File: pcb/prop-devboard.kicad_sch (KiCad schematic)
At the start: 0 parts

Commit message: Initial work on PCB
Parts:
- added C10, C7: 100nF, Capacitor_SMD:C_0402_1005Metric, symbol Device:C
- added C3, C4: 10pF, Capacitor_SMD:C_0402_1005Metric, symbol Device:C
- added C5, C6: 12pF, Capacitor_SMD:C_0402_1005Metric, symbol Device:C
- added R3: 10k, Resistor_SMD:R_0402_1005Metric, symbol Device:R
- added SW1: SW_Push, Button_Switch_SMD:SW_SPST_B3U-1000P, symbol Switch:SW_Push
- added U1: STM32G0B1CBT6, Package_QFP:LQFP-48_7x7mm_P0.5mm, symbol MCU_ST_STM32G0:STM32G0B1CBTx
- added Y1: 32.768 KHz, 10ppm, 12.5pf, Crystal:Crystal_SMD_3215-2Pin_3.2x1.5mm, symbol Device:Crystal
- added Y2: 8 MHz, 10ppm, 10pf, Crystal:Crystal_SMD_3225-4Pin_3.2x2.5mm, symbol Device:Crystal_GND24
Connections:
- new net +3V3: C7.1, R3.1, U1.6 (VDD)
- new net GND: C10.1, C3.2, C4.2, C5.1, C6.2, C7.2, SW1.1, U1.7 (VSS), Y2.2, Y2.4
- new net NRST: C10.2, R3.2, SW1.2, U1.10 (PF2)
- new net OSC32_IN: C5.2, U1.2 (PC14), Y1.2
- new net OSC32_OUT: C6.1, U1.3 (PC15), Y1.1
- new net OSC_IN: C3.1, U1.8 (PF0), Y2.1
- new net OSC_OUT: C4.1, U1.9 (PF1), Y2.3
- new net SWCLK: U1.36 (PA14)
- new net SWDIO: U1.35 (PA13)
- new net UART_RX: U1.32 (PA10/UCPD1_DBCC2)
- new net UART_TX: U1.29 (PA9/UCPD1_DBCC1)
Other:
- added sheet Connectors (connectors.kicad_sch)
- added sheet Power (power.kicad_sch)

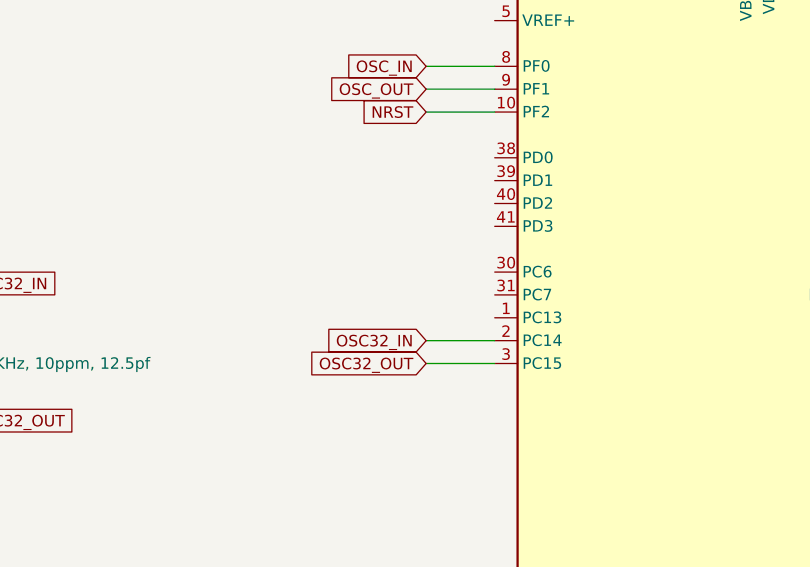
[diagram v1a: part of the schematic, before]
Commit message: Added CubeMX template, and more schematics work
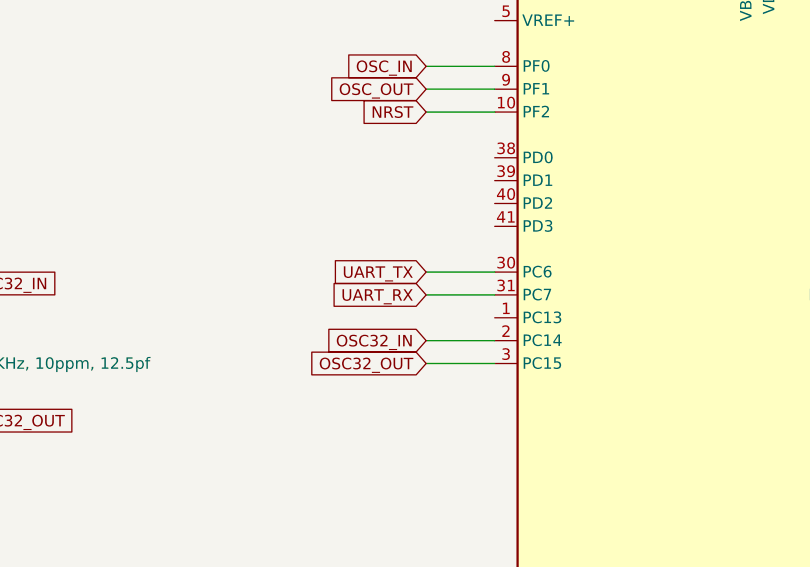
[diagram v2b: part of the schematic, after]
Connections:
- net UART_RX: now also U1.31 (PC7)
- net UART_TX: now also U1.30 (PC6)
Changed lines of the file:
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@@
+	(wire
+		(pts
+			(xy 189.23 74.93) (xy 196.85 74.93)
+		)
+		(stroke
+			(width 0)
+			(type default)
+		)
+	)
 	(wire
 		(pts
@@
 	(wire
 		(pts
+			(xy 189.23 77.47) (xy 196.85 77.47)
+		)
+		(stroke
+			(width 0)
+			(type default)
+		)
+	)
+	(wire
+		(pts
 			(xy 227.33 27.94) (xy 227.33 31.75)
 		)
@@
 		)
 	)
+	(global_label "UART_RX"
+		(shape input)
+		(at 189.23 77.47 180)
+		(fields_autoplaced yes)
+		(effects
+			(font
+				(size 1.27 1.27)
+			)
+			(justify right)
+		)
+		(property "Intersheetrefs" "${INTERSHEET_REFS}"
+			(at 178.141 77.47 0)
+			(effects
+				(font
+					(size 1.27 1.27)
+				)
+				(justify right)
+				(hide yes)
+			)
+		)
+	)
 	(global_label "NRST"
 		(shape input)
@@
 				(hide yes)
 			)
+		)
+	)
+	(global_label "UART_TX"
+		(shape input)
+		(at 189.23 74.93 180)
+		(fields_autoplaced yes)
+		(effects
+			(font
+				(size 1.27 1.27)
+			)
+			(justify right)
+		)
+		(property "Intersheetrefs" "${INTERSHEET_REFS}"
+			(at 178.4434 74.93 0)
+			(effects
+				(font
+					(size 1.27 1.27)
+				)
+				(justify right)
+				(hide yes)
+			)

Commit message: Lots of work on schematics
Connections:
- net UART_RX: no longer U1.32 (PA10/UCPD1_DBCC2)
- net UART_TX: no longer U1.29 (PA9/UCPD1_DBCC1)
- net ANALOG0: now reaches U1.11 (PA0)
- net ANALOG1: now reaches U1.12 (PA1)
- net ANALOG2: now reaches U1.13 (PA2)
- net ANALOG3: now reaches U1.14 (PA3)
- net ANALOG4: now reaches U1.15 (PA4)
- net ANALOG5: now reaches U1.16 (PA5)
- net SPI_MISO: now reaches U1.21 (PB2)
- net SPI_SCK: now reaches U1.22 (PB10)
- net SPI_MOSI: now reaches U1.23 (PB11)
- net I2C2_SCL: now reaches U1.25 (PB13)
- net I2C2_SDA: now reaches U1.26 (PB14)
- net I2C3_SCL: now reaches U1.42 (PB3)
- net I2C3_SDA: now reaches U1.43 (PB4)
- new net I2C1_SCL: U1.29 (PA9/UCPD1_DBCC1)
- new net I2C1_SDA: U1.32 (PA10/UCPD1_DBCC2)

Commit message: Mostly finished PCB layout
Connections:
- net DIGITAL5: now reaches U1.33 (PA9/PA11)
- net DIGITAL6: now reaches U1.34 (PA10/PA12)
- net DIGITAL9: now reaches U1.37 (PA15)
- net DIGITAL10: now reaches U1.38 (PD0)
- net DIGITAL11: now reaches U1.39 (PD1)
- net DIGITAL12: now reaches U1.40 (PD2)
- net DIGITAL13: now reaches U1.41 (PD3)
- net SWCLK renamed BOOT0

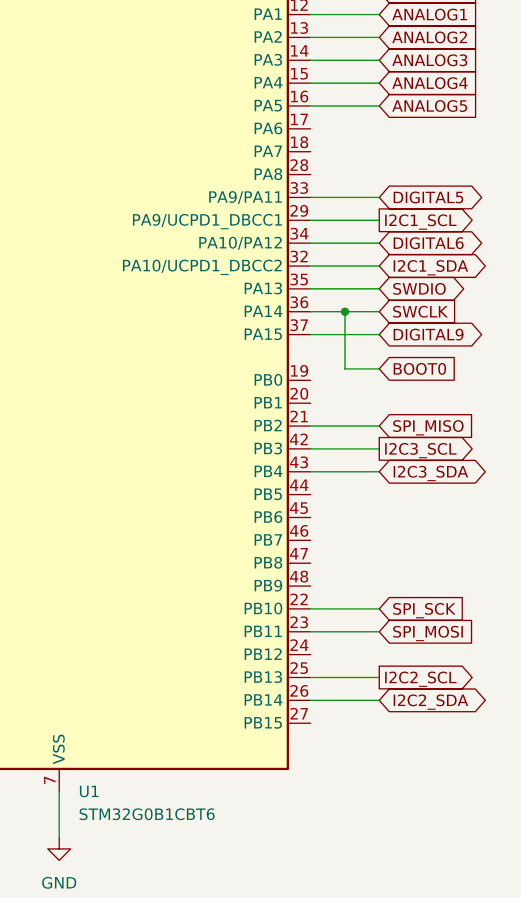
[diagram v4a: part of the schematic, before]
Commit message: Added USB support
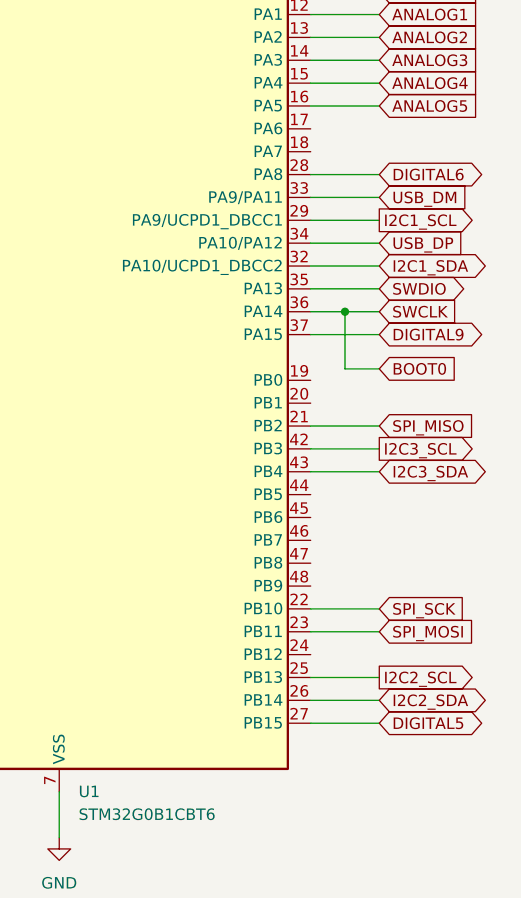
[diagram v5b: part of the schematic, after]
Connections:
- net DIGITAL5: now also U1.27 (PB15); no longer U1.33 (PA9/PA11)
- net DIGITAL6: now also U1.28 (PA8); no longer U1.34 (PA10/PA12)
- new net USB_DM: U1.33 (PA9/PA11)
- new net USB_DP: U1.34 (PA10/PA12)
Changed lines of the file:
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@@
+	(wire
+		(pts
+			(xy 252.73 67.31) (xy 260.35 67.31)
+		)
+		(stroke
+			(width 0)
+			(type default)
+		)
+	)
 	(wire
 		(pts
@@
 	(wire
 		(pts
+			(xy 252.73 128.27) (xy 260.35 128.27)
+		)
+		(stroke
+			(width 0)
+			(type default)
+		)
+	)
+	(wire
+		(pts
 			(xy 189.23 62.23) (xy 196.85 62.23)
 		)
@@
 		(property "Intersheetrefs" "${INTERSHEET_REFS}"
 			(at 146.8581 118.11 0)
+			(effects
+				(font
+					(size 1.27 1.27)
+				)
+				(justify left)
+				(hide yes)
+			)
+		)
+	)
+	(global_label "DIGITAL6"
+		(shape bidirectional)
+		(at 260.35 67.31 0)
+		(fields_autoplaced yes)
+		(effects
+			(font
+				(size 1.27 1.27)
+			)
+			(justify left)
+		)
+		(property "Intersheetrefs" "${INTERSHEET_REFS}"
+			(at 272.4899 67.31 0)
 			(effects
 				(font
@@
 		)
 	)
-	(global_label "DIGITAL6"
-		(shape bidirectional)
-		(at 260.35 74.93 0)
-		(fields_autoplaced yes)
-		(effects
-			(font
-				(size 1.27 1.27)
-			)
-			(justify left)
-		)
-		(property "Intersheetrefs" "${INTERSHEET_REFS}"
-			(at 272.4899 74.93 0)
-			(effects
-				(font
-					(size 1.27 1.27)
-				)
-				(justify left)
-				(hide yes)
-			)
-		)
-	)
 	(global_label "I2C3_SCL"
 		(shape output)
@@
 		)
 	)
+	(global_label "USB_DP"
+		(shape input)
+		(at 260.35 74.93 0)
+		(fields_autoplaced yes)
+		(effects
+			(font
+				(size 1.27 1.27)
+			)
+			(justify left)
+		)
+		(property "Intersheetrefs" "${INTERSHEET_REFS}"
+			(at 270.6528 74.93 0)
+			(effects
+				(font
+					(size 1.27 1.27)
+				)
+				(justify left)
+				(hide yes)
+			)
+		)
+	)
 	(global_label "ANALOG3"
 		(shape input)
@@
 		(property "Intersheetrefs" "${INTERSHEET_REFS}"
 			(at 271.681 57.15 0)
+			(effects
+				(font
+					(size 1.27 1.27)
+				)
+				(justify left)
+				(hide yes)
+			)
+		)
+	)
+	(global_label "DIGITAL5"
+		(shape bidirectional)
+		(at 260.35 128.27 0)
+		(fields_autoplaced yes)
+		(effects
+			(font
+				(size 1.27 1.27)
+			)
+			(justify left)
+		)
+		(property "Intersheetrefs" "${INTERSHEET_REFS}"
+			(at 272.4899 128.27 0)
 			(effects
 				(font
@@
 		)
 	)
-	(global_label "DIGITAL5"
-		(shape bidirectional)
-		(at 260.35 69.85 0)
-		(fields_autoplaced yes)
-		(effects
-			(font
-				(size 1.27 1.27)
-			)
-			(justify left)
-		)
-		(property "Intersheetrefs" "${INTERSHEET_REFS}"
-			(at 272.4899 69.85 0)
-			(effects
-				(font
-					(size 1.27 1.27)
-				)
-				(justify left)
-				(hide yes)
-			)
-		)
-	)
 	(global_label "I2C2_SCL"
 		(shape output)
@@
 			(effects
 				(font
+					(size 1.27 1.27)
+				)
+				(justify left)
+				(hide yes)
+			)
+		)
+	)
+	(global_label "USB_DM"
+		(shape input)
+		(at 260.35 69.85 0)
+		(fields_autoplaced yes)
+		(effects
+			(font
+				(size 1.27 1.27)
+			)
+			(justify left)
+		)
+		(property "Intersheetrefs" "${INTERSHEET_REFS}"
+			(at 270.8342 69.85 0)
+			(effects
+				(font

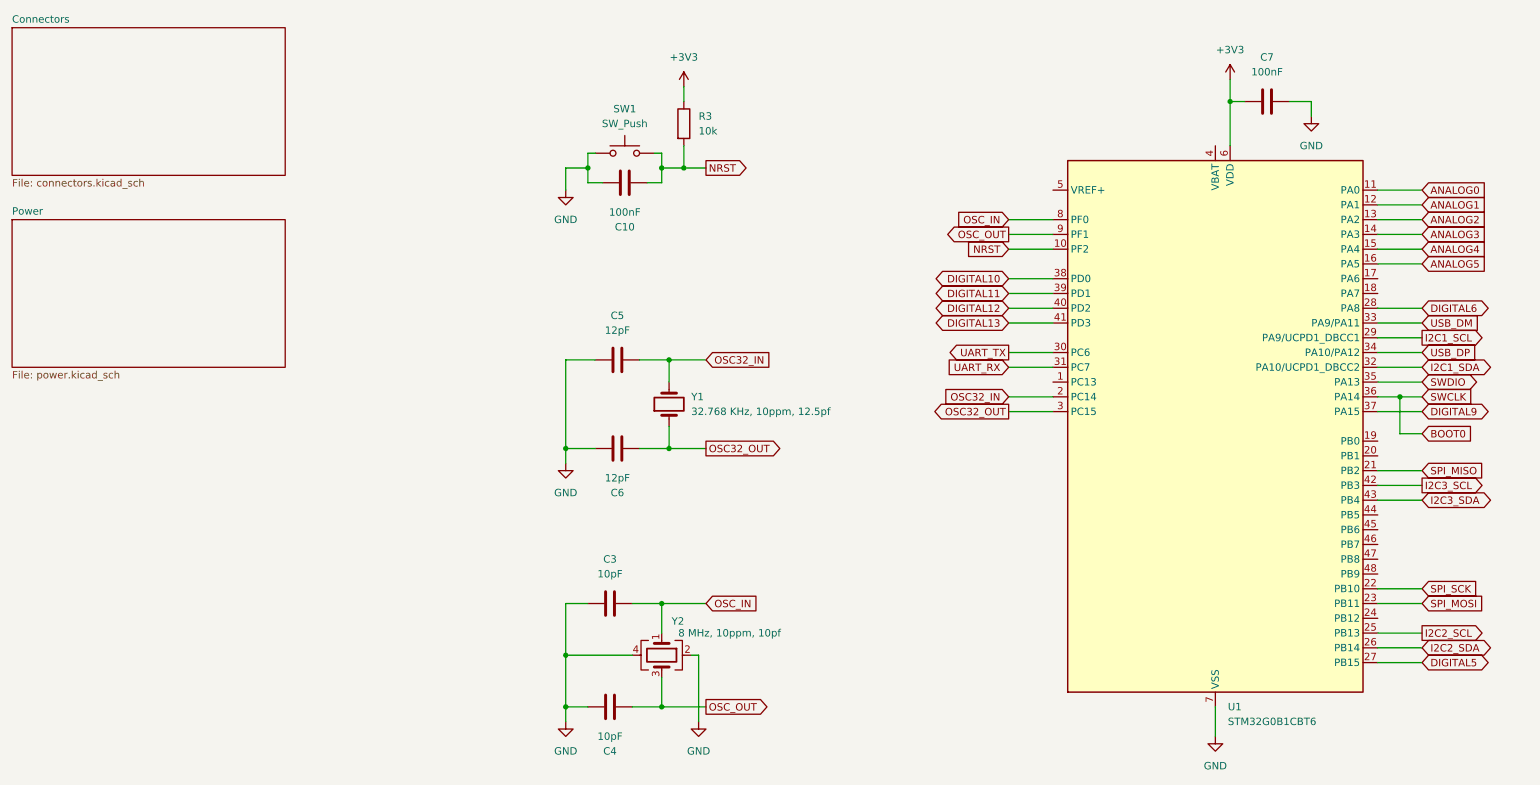
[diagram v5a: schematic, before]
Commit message: Added power and status LEDs to the design
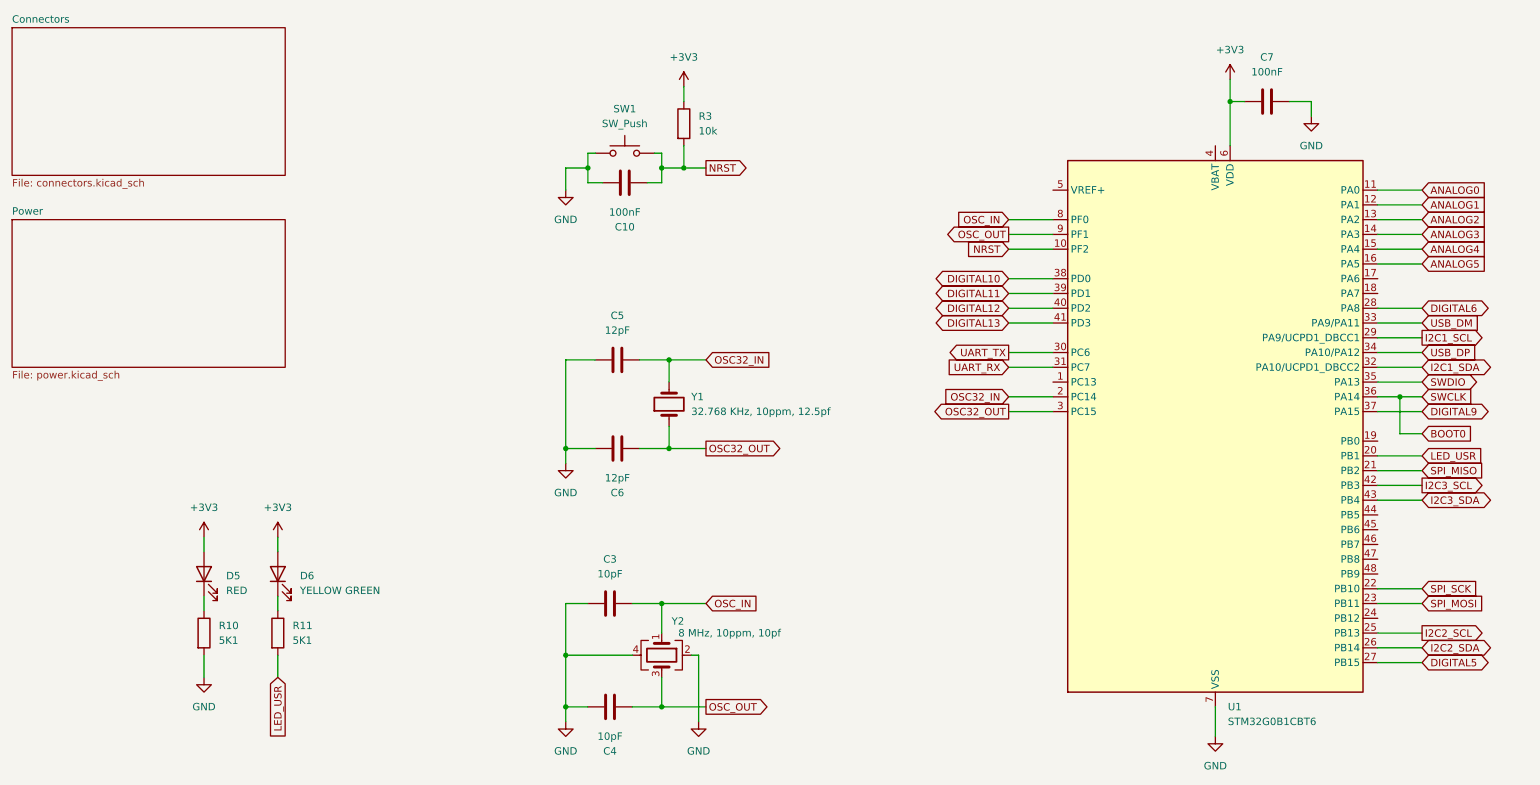
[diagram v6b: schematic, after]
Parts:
- added D5: RED, LED_SMD:LED_0402_1005Metric, symbol Device:LED
- added D6: YELLOW GREEN, LED_SMD:LED_0402_1005Metric, symbol Device:LED
- added R10, R11: 5K1, Resistor_SMD:R_0402_1005Metric, symbol Device:R
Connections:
- net +3V3: now also D5.2 (A), D6.2 (A)
- net GND: now also R10.2
- net LED_USR: now reaches U1.20 (PB1)
- net LED_USR: now also R11.2
- new net: D6.1 (K), R11.1
- new net: D5.1 (K), R10.1

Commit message: Fixed MCU power pins not being connected correctly
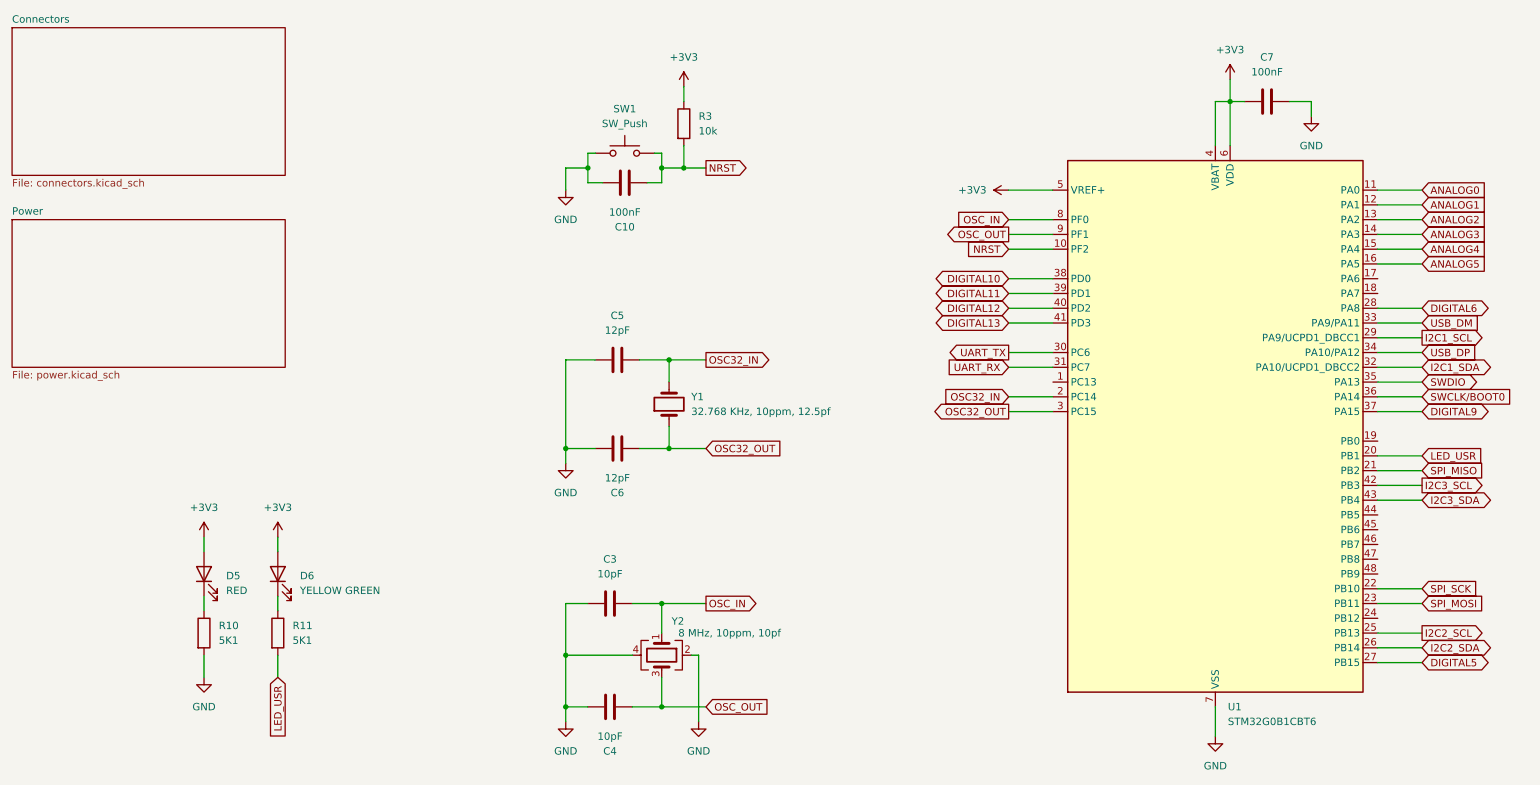
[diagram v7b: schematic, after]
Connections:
- net +3V3: now also U1.4 (VBAT), U1.5 (VREF+)
- net BOOT0 renamed SWCLK/BOOT0
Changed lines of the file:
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@@
 	(paper "A4")
-	(junction
-		(at 256.54 82.55)
-		(diameter 0)
-		(color 0 0 0 0)
-	)
 	(junction
 		(at 129.54 135.89)
@@
 	(wire
 		(pts
+			(xy 224.79 39.37) (xy 224.79 31.75)
+		)
+		(stroke
+			(width 0)
+			(type default)
+		)
+	)
+	(wire
+		(pts
 			(xy 50.8 106.68) (xy 50.8 109.22)
 		)
@@
 	(wire
 		(pts
-			(xy 260.35 88.9) (xy 256.54 88.9)
-		)
-		(stroke
-			(width 0)
-			(type default)
-		)
-	)
-	(wire
-		(pts
 			(xy 189.23 74.93) (xy 196.85 74.93)
 		)
@@
 	(wire
 		(pts
-			(xy 256.54 88.9) (xy 256.54 82.55)
-		)
-		(stroke
-			(width 0)
-			(type default)
-		)
-	)
-	(wire
-		(pts
 			(xy 129.54 43.18) (xy 133.35 43.18)
 		)
@@
 	(wire
 		(pts
+			(xy 224.79 31.75) (xy 227.33 31.75)
+		)
+		(stroke
+			(width 0)
+			(type default)
+		)
+	)
+	(wire
+		(pts
 			(xy 116.84 45.72) (xy 119.38 45.72)
 		)
@@
 	(wire
 		(pts
-			(xy 256.54 82.55) (xy 260.35 82.55)
+			(xy 252.73 82.55) (xy 260.35 82.55)
 		)
 		(stroke
@@
 	(wire
 		(pts
+			(xy 189.23 46.99) (xy 196.85 46.99)
+		)
+		(stroke
+			(width 0)
+			(type default)
+		)
+	)
+	(wire
+		(pts
 			(xy 237.49 31.75) (xy 241.3 31.75)
 		)
@@
 	(wire
 		(pts
-			(xy 252.73 82.55) (xy 256.54 82.55)
-		)
-		(stroke
-			(width 0)
-			(type default)
-		)
-	)
-	(wire
-		(pts
 			(xy 252.73 128.27) (xy 260.35 128.27)
 		)
@@
 	)
 	(global_label "OSC_IN"
-		(shape input)
+		(shape output)
 		(at 137.16 118.11 0)
 		(fields_autoplaced yes)
@@
 		)
 	)
-	(global_label "BOOT0"
+	(global_label "OSC_OUT"
 		(shape input)
-		(at 260.35 88.9 0)
-		(fields_autoplaced yes)
-		(effects
-			(font
-				(size 1.27 1.27)
-			)
-			(justify left)
-		)
-		(property "Intersheetrefs" "${INTERSHEET_REFS}"
-			(at 269.4433 88.9 0)
-			(effects
-				(font
-					(size 1.27 1.27)
-				)
-				(justify left)
-				(hide yes)
-			)
-		)
-	)
-	(global_label "OSC_OUT"
-		(shape output)
 		(at 137.16 135.89 0)
 		(fields_autoplaced yes)
@@
 	)
 	(global_label "OSC32_OUT"
-		(shape output)
+		(shape input)
 		(at 137.16 91.44 0)
 		(fields_autoplaced yes)
@@
 		)
 	)
-	(global_label "SWCLK"
+	(global_label "SWCLK{slash}BOOT0"
 		(shape input)
 		(at 260.35 82.55 0)
@@
 		)
 		(property "Intersheetrefs" "${INTERSHEET_REFS}"
-			(at 269.5642 82.55 0)
+			(at 277.0028 82.55 0)
 			(effects
 				(font
@@
 	)
 	(global_label "OSC32_IN"
-		(shape input)
+		(shape output)
 		(at 137.16 76.2 0)
 		(fields_autoplaced yes)
@@
 					(unit 1)
 				)
+			)
+		)
+	)
+	(symbol
+		(lib_id "power:+3V3")
+		(at 189.23 46.99 90)
+		(unit 1)
+		(exclude_from_sim no)
+		(in_bom yes)
+		(on_board yes)
+		(dnp no)
+		(fields_autoplaced yes)
+		(property "Reference" "#PWR048"
+			(at 193.04 46.99 0)
+			(effects
+				(font
+					(size 1.27 1.27)
+				)
+				(hide yes)
+			)
+		)
+		(property "Value" "+3V3"
+			(at 185.42 46.9899 90)
+			(effects
+				(font
+					(size 1.27 1.27)
+				)
+				(justify left)
+			)
+		)
+		(property "Footprint" ""
+			(at 189.23 46.99 0)
+			(effects
+				(font
+					(size 1.27 1.27)
+				)
+				(hide yes)
+			)
+		)
+		(property "Datasheet" ""
+			(at 189.23 46.99 0)
+			(effects
+				(font
+					(size 1.27 1.27)
+				)
+				(hide yes)
+			)
+		)
+		(property "Description" "Power symbol creates a global label with name \"+3V3\""
+			(at 189.23 46.99 0)
+			(effects
+				(font
+					(size 1.27 1.27)
+				)
+				(hide yes)
+			)
+		)
+		(pin "1"
+		)
+		(instances
+			(project "prop-devboard"
+				(path "/7abe3e47-948c-4c3d-84e7-3a59f7cbe9b7"
+					(reference "#PWR048")
+					(unit 1)
+				)
